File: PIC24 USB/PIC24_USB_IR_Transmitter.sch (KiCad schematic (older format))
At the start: 26 parts, among them CON1 USB-MINI-B, P1 CONN_6, P2 CONN_4, P3 CONN_6, P4 CONN_6, P5 CONN_4, P6 CONN_1, P7 CONN_8, Q1 2N7002, U1 1586-PIC18F4550-I/PT, X1 12Mhz

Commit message: corrected wrong pin name to VUSB on pic24
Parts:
- removed U1: 1586-PIC18F4550-I/PT, bittenbybytes/axylf, symbol 1586-PIC18F4550-I/PT
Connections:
- wire segments 131 -> 127
- no-connect marks 21 -> 4
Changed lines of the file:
@@
-EESchema Schematic File Version 2  date 18.01.2014 12:00:07
+EESchema Schematic File Version 2  date 31.07.2014 13:18:16
 LIBS:power
 LIBS:device
@@
 LIBS:valves
 LIBS:CircuitHub
-LIBS:pic18_USB_IR_Transmitter-cache
+LIBS:microchip_hele
 EELAYER 27 0
 EELAYER END
@@
 Sheet 1 1
 Title ""
-Date "18 jan 2014"
+Date "31 jul 2014"
 Rev ""
 Comp ""
@@
 Wire Wire Line
 	9600 4950 9600 5000
-NoConn ~ 8050 4800
-NoConn ~ 8050 4900
-NoConn ~ 5550 4900
-NoConn ~ 5550 5000
 Text GLabel 2150 5450 2    60   Output ~ 0
 ~MCLR~
@@
 	5450 5900 5550 5900
 Wire Wire Line
-	8050 3800 8150 3800
-Wire Wire Line
-	8150 3800 8150 3300
-Wire Wire Line
 	8150 3300 8450 3300
-Wire Wire Line
-	5550 3800 5500 3800
-Wire Wire Line
-	5500 3800 5500 3200
-Wire Wire Line
-	5500 3200 8450 3200
 Wire Wire Line
 	8450 3400 8350 3400
@@
 Wire Wire Line
 	5450 4000 5550 4000
-NoConn ~ 5550 3900
-NoConn ~ 5550 4800
-NoConn ~ 8050 4100
-NoConn ~ 8050 4200
-NoConn ~ 8050 4300
-NoConn ~ 8050 4400
-NoConn ~ 8050 5000
-NoConn ~ 8050 5500
-NoConn ~ 8050 5700
-NoConn ~ 8050 5600
-NoConn ~ 8050 5800
-NoConn ~ 8050 5900
 $Comp
 L +5V #PWR028
@@
 Wire Wire Line
 	3800 4250 3800 4200
-NoConn ~ 5550 5200
-$Comp
-L 1586-PIC18F4550-I/PT U1
-U 1 1 52D4664F
-P 5750 3700
-F 0 "U1" H 5750 3730 60  0000 L CNN
-F 1 "1586-PIC18F4550-I/PT" H 5750 1370 60  0000 L CNN
-F 2 "bittenbybytes/axylf" H 5750 4000 60  0001 L CNN
-F 3 "https://circuithub.com/parts/MICROCHIP/PIC18F4550-I%2FPT/documents" H 5750 4100 60  0001 L CNN
-F 4 "1586" H 5750 4200 60  0001 L CNN "CircuitHubID"
-F 5 "bittenbybytes/dlggy" H 5750 4300 60  0001 L CNN "symbolURN"
-F 6 "6fcab3e7681bbab4137038658c0f0c25a00fc3ae" H 5750 4400 60  0001 L CNN "symbolRevision"
-F 7 "cbd665ea3e7566542faf2266d4c1fac7b0158e08" H 5750 4500 60  0001 L CNN "footprintRevision"
-	1    5750 3700
-	1    0    0    -1
-$EndComp
 Text Label 8200 3200 0    60   ~ 0
 RX
@@
 Wire Wire Line
 	3600 4900 4100 4900
+Wire Wire Line
+	8450 3200 8150 3200
 $EndSCHEMATC

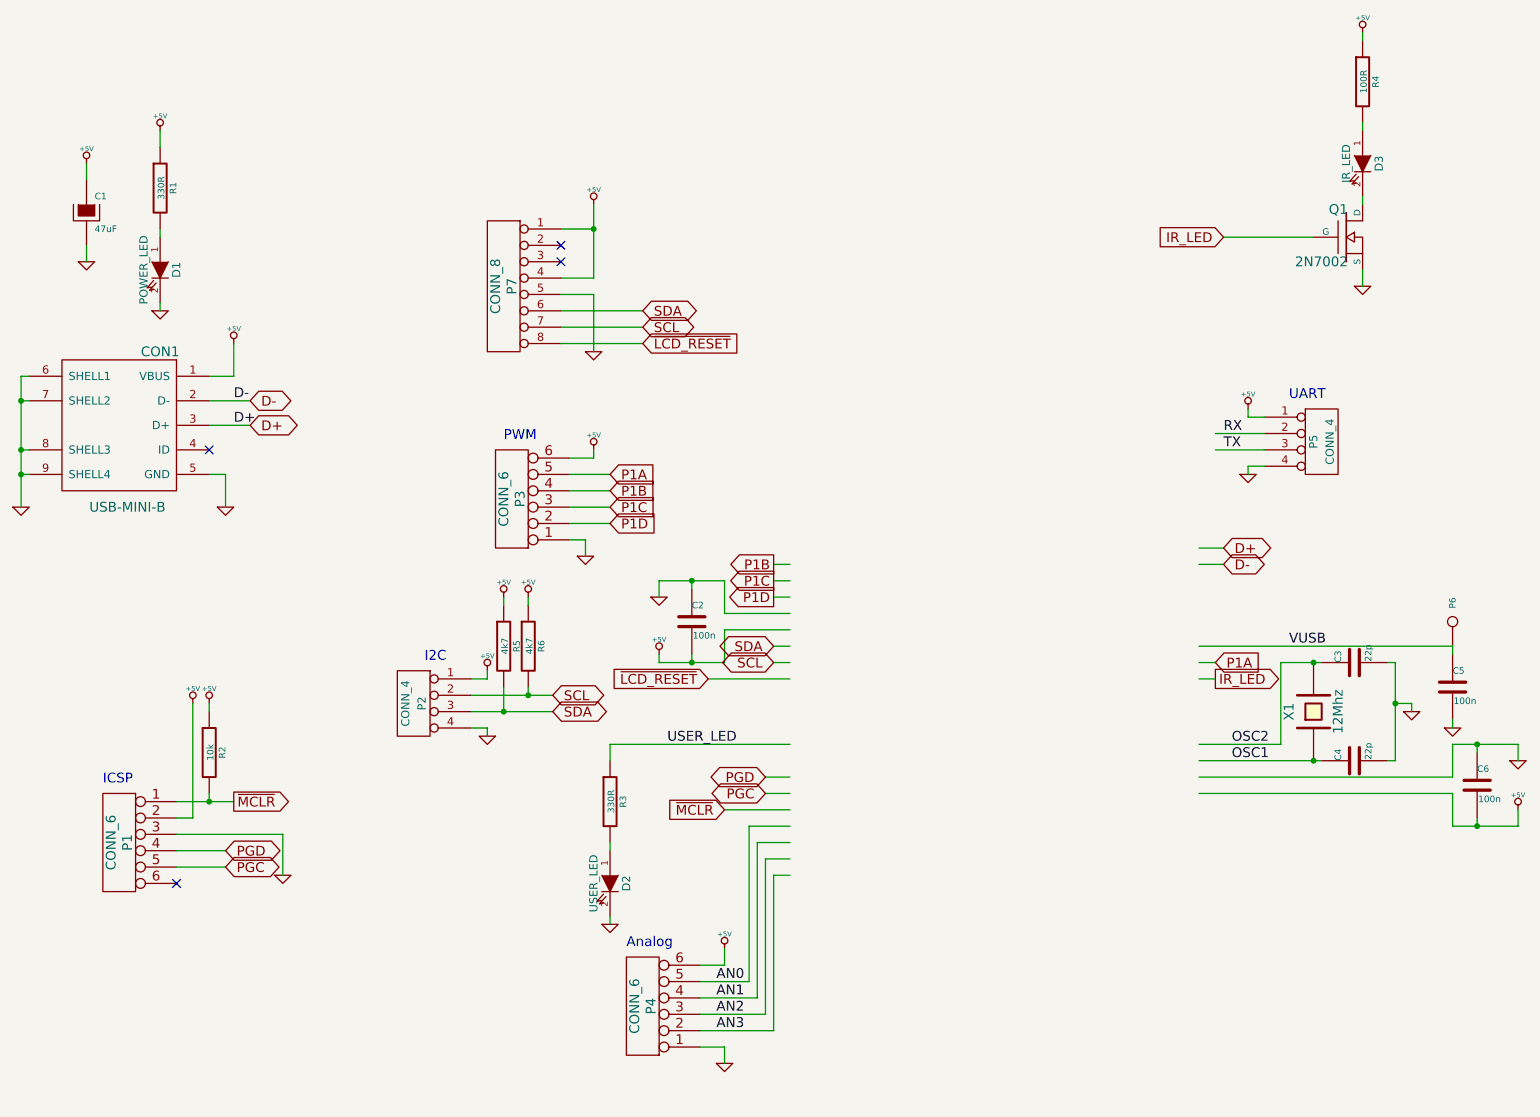
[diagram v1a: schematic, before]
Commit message: inserted pic24 into schematic
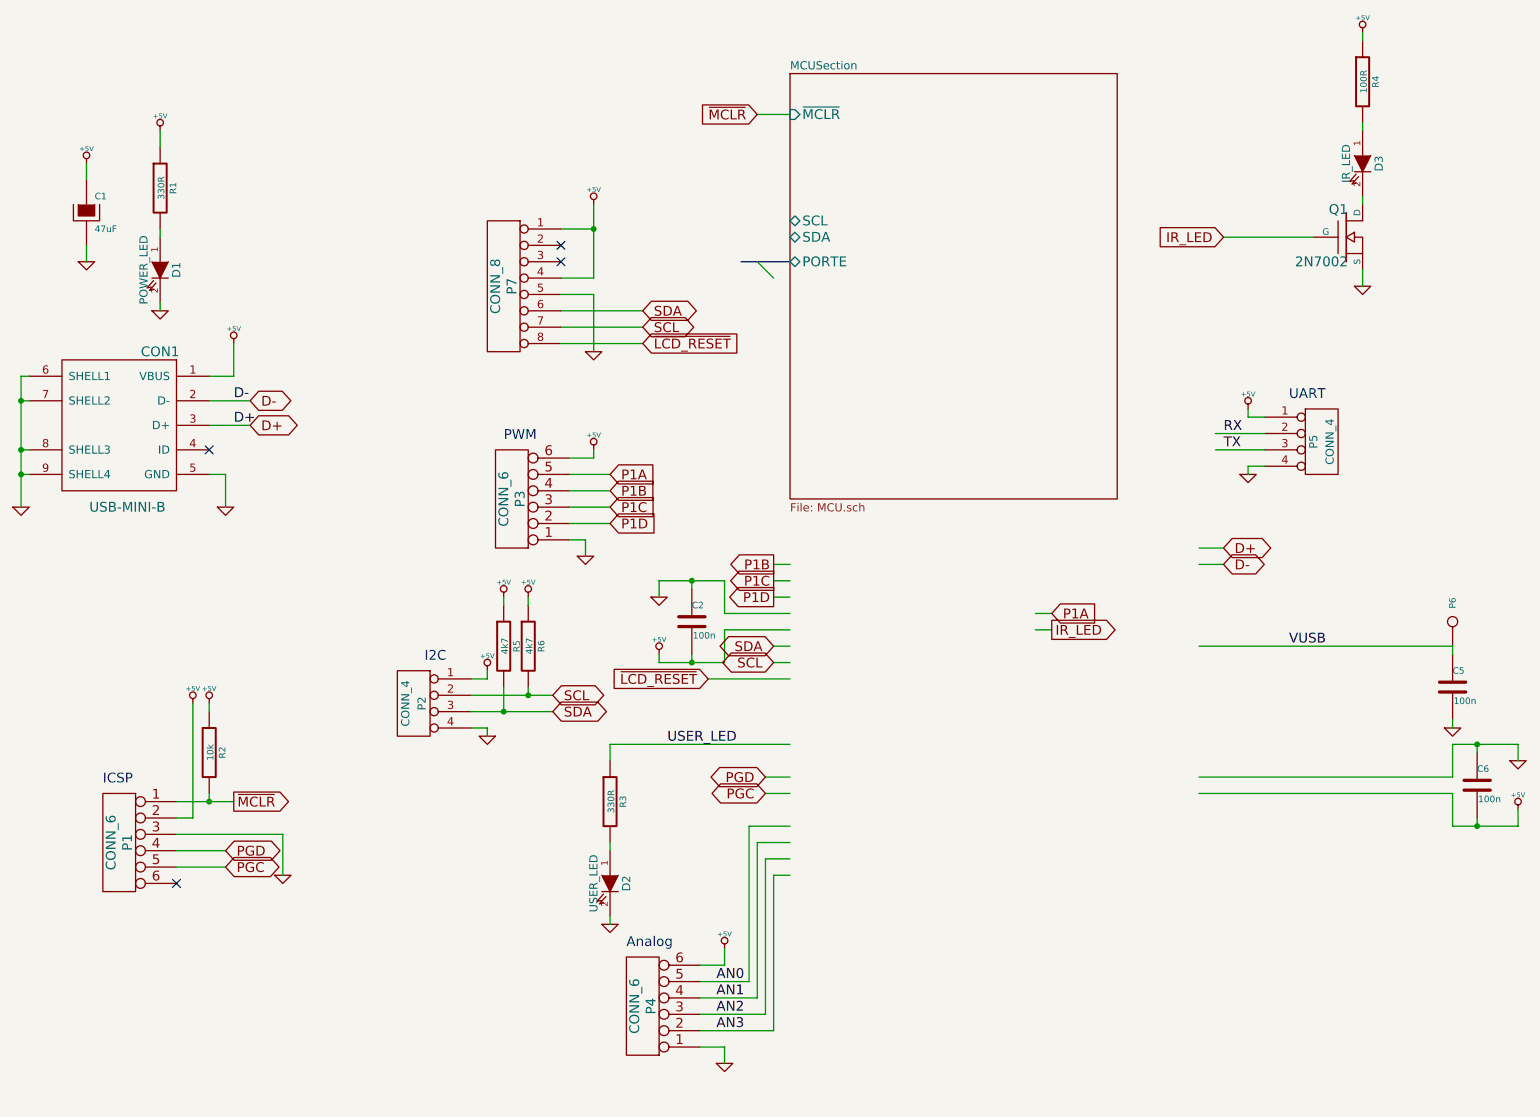
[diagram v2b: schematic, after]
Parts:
- removed C3, C4: 22p, symbol C
- removed X1: 12Mhz, symbol CRYSTAL
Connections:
- net labels removed: OSC1, OSC2
- wire segments 127 -> 118
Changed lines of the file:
@@
-EESchema Schematic File Version 2  date 31.07.2014 13:18:16
+EESchema Schematic File Version 2  date 31.07.2014 14:53:52
 LIBS:power
 LIBS:device
@@
 $Descr A4 11693 8268
 encoding utf-8
-Sheet 1 1
+Sheet 1 2
 Title ""
 Date "31 jul 2014"
@@
 Wire Wire Line
 	5400 5300 5550 5300
-Text GLabel 5150 5500 0    60   Input ~ 0
+Text GLabel 5350 1250 0    60   Input ~ 0
 ~MCLR~
-Wire Wire Line
-	5150 5500 5550 5500
-$Comp
-L CRYSTAL X1
-U 1 1 52D4526C
-P 8750 4900
-F 0 "X1" H 8750 5050 60  0000 C CNN
-F 1 "12Mhz" H 8750 4750 60  0000 C CNN
-F 2 "" H 8750 4900 60  0000 C CNN
-F 3 "" H 8750 4900 60  0000 C CNN
-	1    8750 4900
-	0    -1   -1   0
-$EndComp
-Wire Wire Line
-	8050 5100 8550 5100
-Wire Wire Line
-	8550 5100 8550 4600
-Wire Wire Line
-	8550 4600 8800 4600
-Wire Wire Line
-	8050 5200 8800 5200
-$Comp
-L C C3
-U 1 1 52D45390
-P 9000 4600
-F 0 "C3" H 9000 4700 40  0000 L CNN
-F 1 "22p" H 9006 4515 40  0000 L CNN
-F 2 "" H 9038 4450 30  0000 C CNN
-F 3 "" H 9000 4600 60  0000 C CNN
-	1    9000 4600
-	0    -1   -1   0
-$EndComp
-Connection ~ 8750 4600
-$Comp
-L C C4
-U 1 1 52D4546D
-P 9000 5200
-F 0 "C4" H 9000 5300 40  0000 L CNN
-F 1 "22p" H 9006 5115 40  0000 L CNN
-F 2 "" H 9038 5050 30  0000 C CNN
-F 3 "" H 9000 5200 60  0000 C CNN
-	1    9000 5200
-	0    -1   -1   0
-$EndComp
-$Comp
-L GND #PWR014
-U 1 1 52D45473
-P 9350 4900
-F 0 "#PWR014" H 9350 4900 30  0001 C CNN
-F 1 "GND" H 9350 4830 30  0001 C CNN
-F 2 "" H 9350 4900 60  0000 C CNN
-F 3 "" H 9350 4900 60  0000 C CNN
-	1    9350 4900
-	1    0    0    -1
-$EndComp
-Connection ~ 8750 5200
-Wire Wire Line
-	9200 4600 9250 4600
-Wire Wire Line
-	9250 4600 9250 5200
-Wire Wire Line
-	9250 5200 9200 5200
-Wire Wire Line
-	9250 4850 9350 4850
-Wire Wire Line
-	9350 4850 9350 4900
-Connection ~ 9250 4850
-Text GLabel 8150 4600 2    60   Input ~ 0
+Text GLabel 7150 4300 2    60   Input ~ 0
 P1A
-Text GLabel 8150 4700 2    60   Output ~ 0
+Text GLabel 7150 4400 2    60   Output ~ 0
 IR_LED
 Text GLabel 8200 2000 0    60   Input ~ 0
@@
 AN3
 Wire Wire Line
-	8050 4600 8150 4600
-Wire Wire Line
-	8050 4700 8150 4700
+	7050 4300 7150 4300
+Wire Wire Line
+	7050 4400 7150 4400
 NoConn ~ 2000 3300
 NoConn ~ 1800 5950
-Text Label 8250 5100 0    60   ~ 0
-OSC2
-Text Label 8250 5200 0    60   ~ 0
-OSC1
 Text Label 4800 5100 0    60   ~ 0
 USER_LED
@@
 Wire Wire Line
 	8450 3200 8150 3200
+$Sheet
+S 5550 1000 2000 2600
+U 53DA26B9
+F0 "MCUSection" 50
+F1 "MCU.sch" 50
+F2 "~MCLR" I L 5550 1250 60
+F3 "SCL" B L 5550 1900 60
+F4 "SDA" B L 5550 2000 60
+F5 "PORTE" B L 5550 2150 60
+$EndSheet
+Wire Wire Line
+	5550 1250 5350 1250
+Wire Bus Line
+	5550 2150 5250 2150
+Entry Wire Line
+	5350 2150 5450 2250
 $EndSCHEMATC

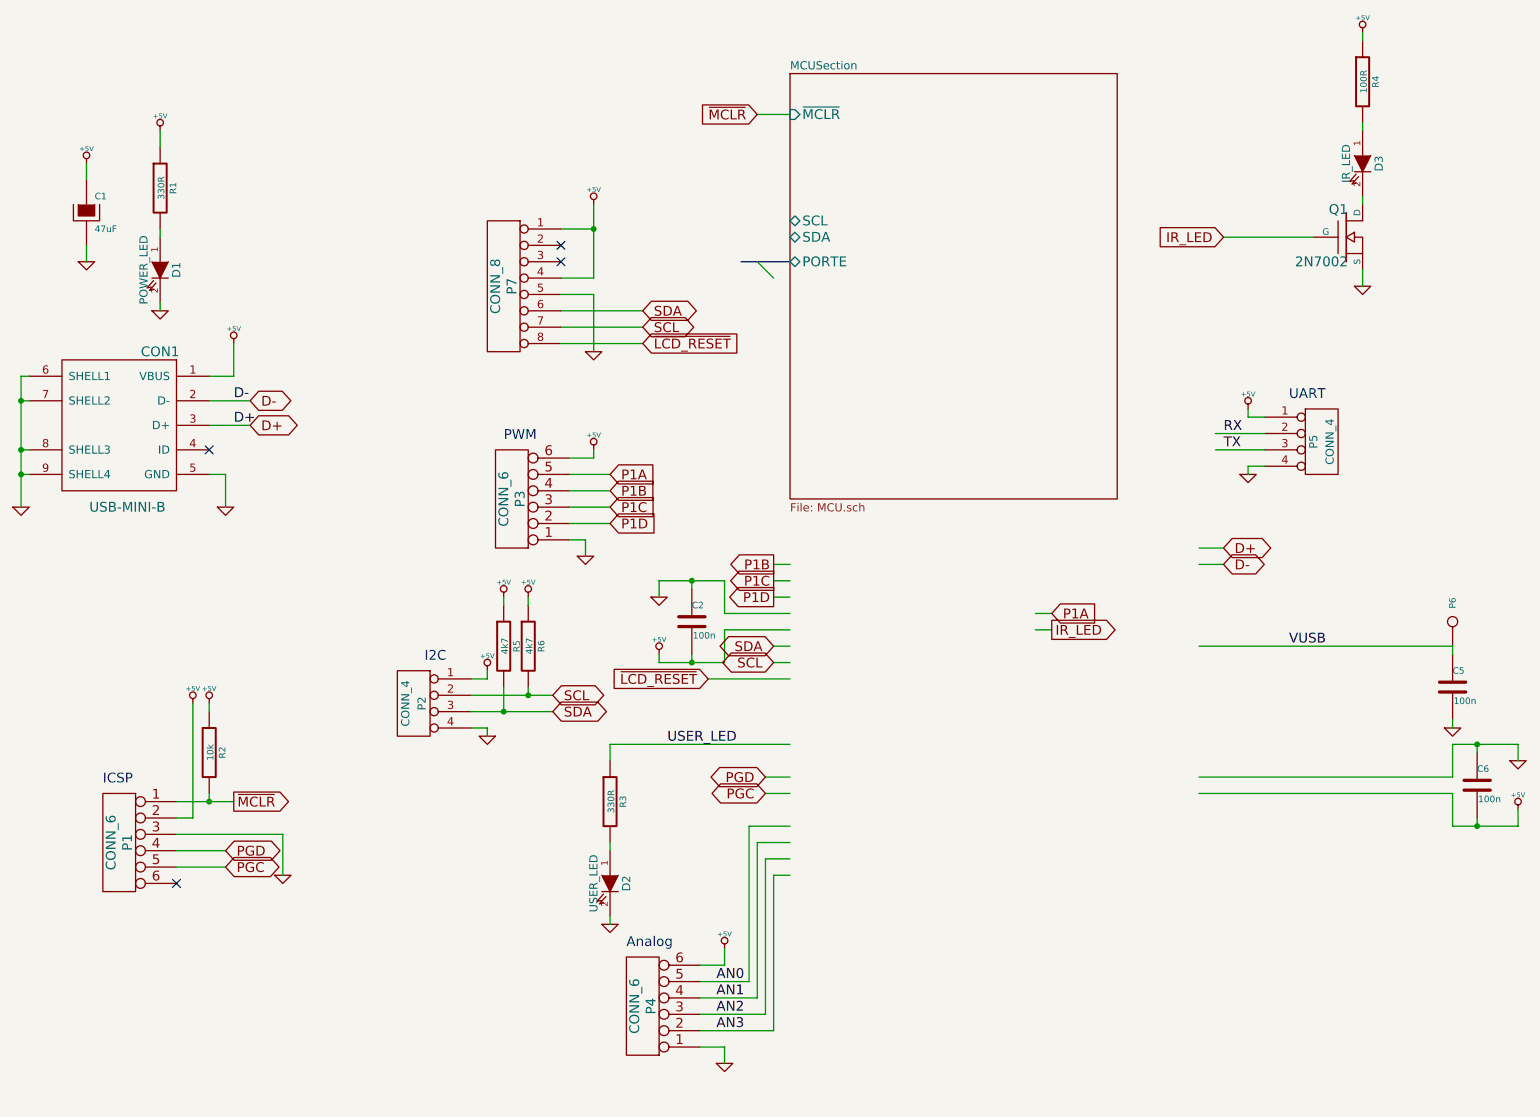
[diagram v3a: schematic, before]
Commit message: inserted some mandatory mcu connecrtion and a bus connection
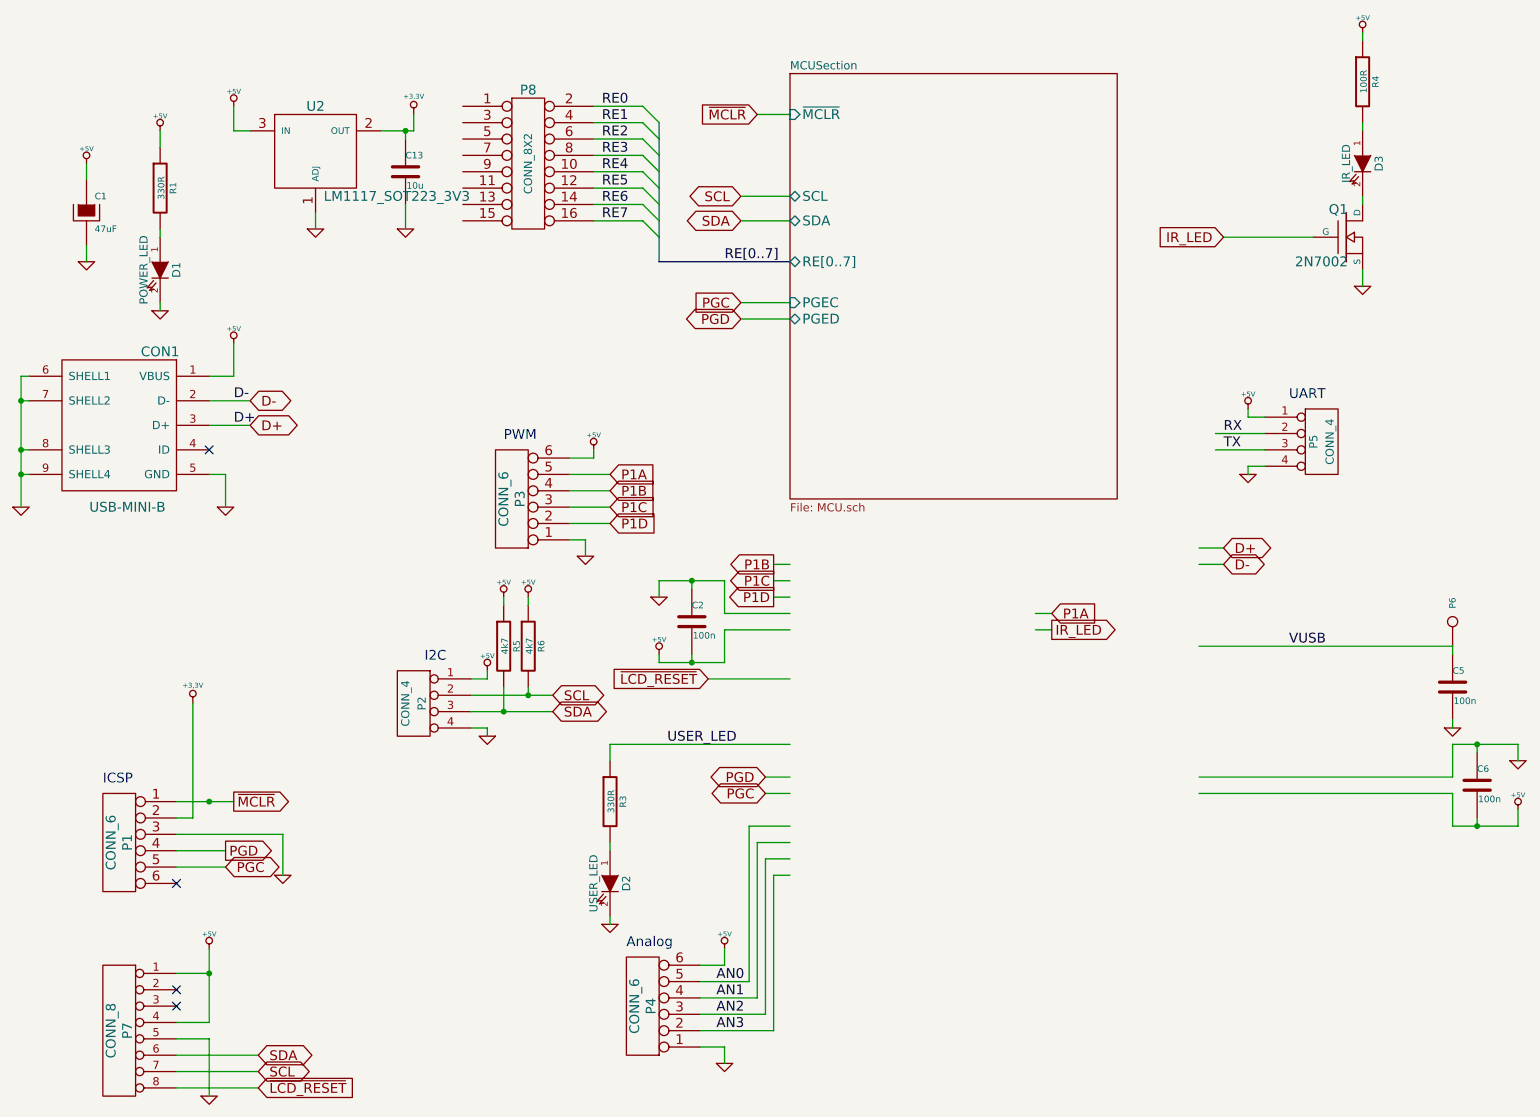
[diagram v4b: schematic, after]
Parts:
- removed R2: 10k, symbol R
- added C13: 10u, ~, symbol C
- added P8: CONN_8X2, symbol CONN_8X2
- added U2: LM1117_SOT223_3V3, ~, symbol LM317_SOT223
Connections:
- net labels added: +3,3V, RE0, RE1, RE2, RE3, RE4, RE5, RE6, RE7, RE[0..7]
- wire segments 118 -> 133
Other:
- moved on the sheet: P7
